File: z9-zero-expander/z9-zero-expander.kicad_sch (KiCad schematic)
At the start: 3 parts, among them J1 Conn_DF40HC3.0-100DP-0.4V51, J2 Conn_01x50, J3 Conn_01x50

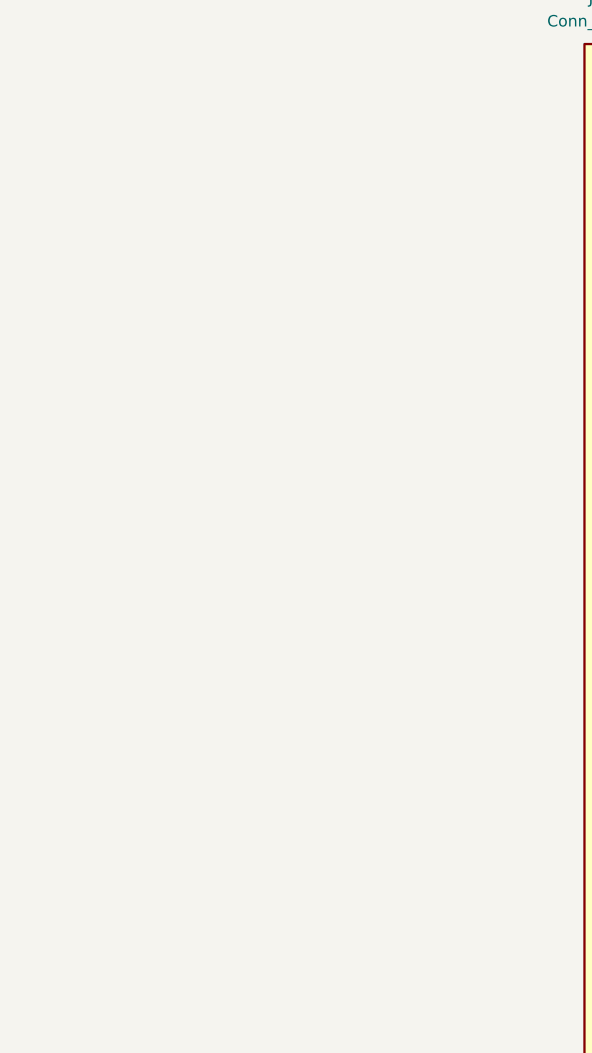
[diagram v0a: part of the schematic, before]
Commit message: z9-zero-expander: migrate to KiCad 10 and add new sub-sheets
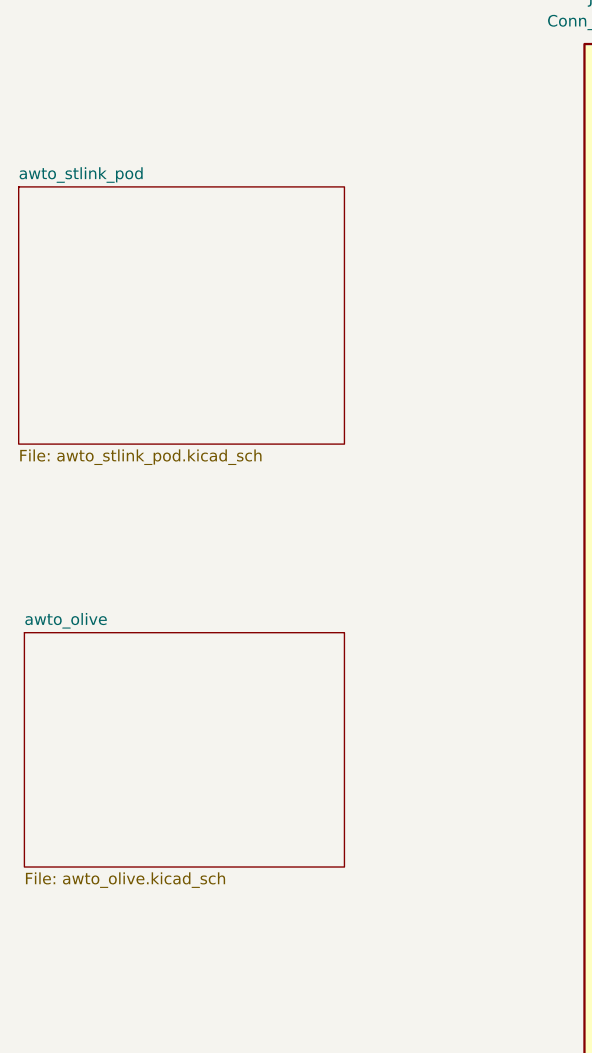
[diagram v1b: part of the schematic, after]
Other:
- added sheet awto_olive (awto_olive.kicad_sch)
- added sheet awto_stlink_pod (awto_stlink_pod.kicad_sch)
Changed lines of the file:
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@@
 (kicad_sch
-	(version 20250114)
+	(version 20260306)
 	(generator "eeschema")
-	(generator_version "9.0")
+	(generator_version "10.0")
 	(paper "A4")
